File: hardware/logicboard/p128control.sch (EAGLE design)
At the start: 13 parts

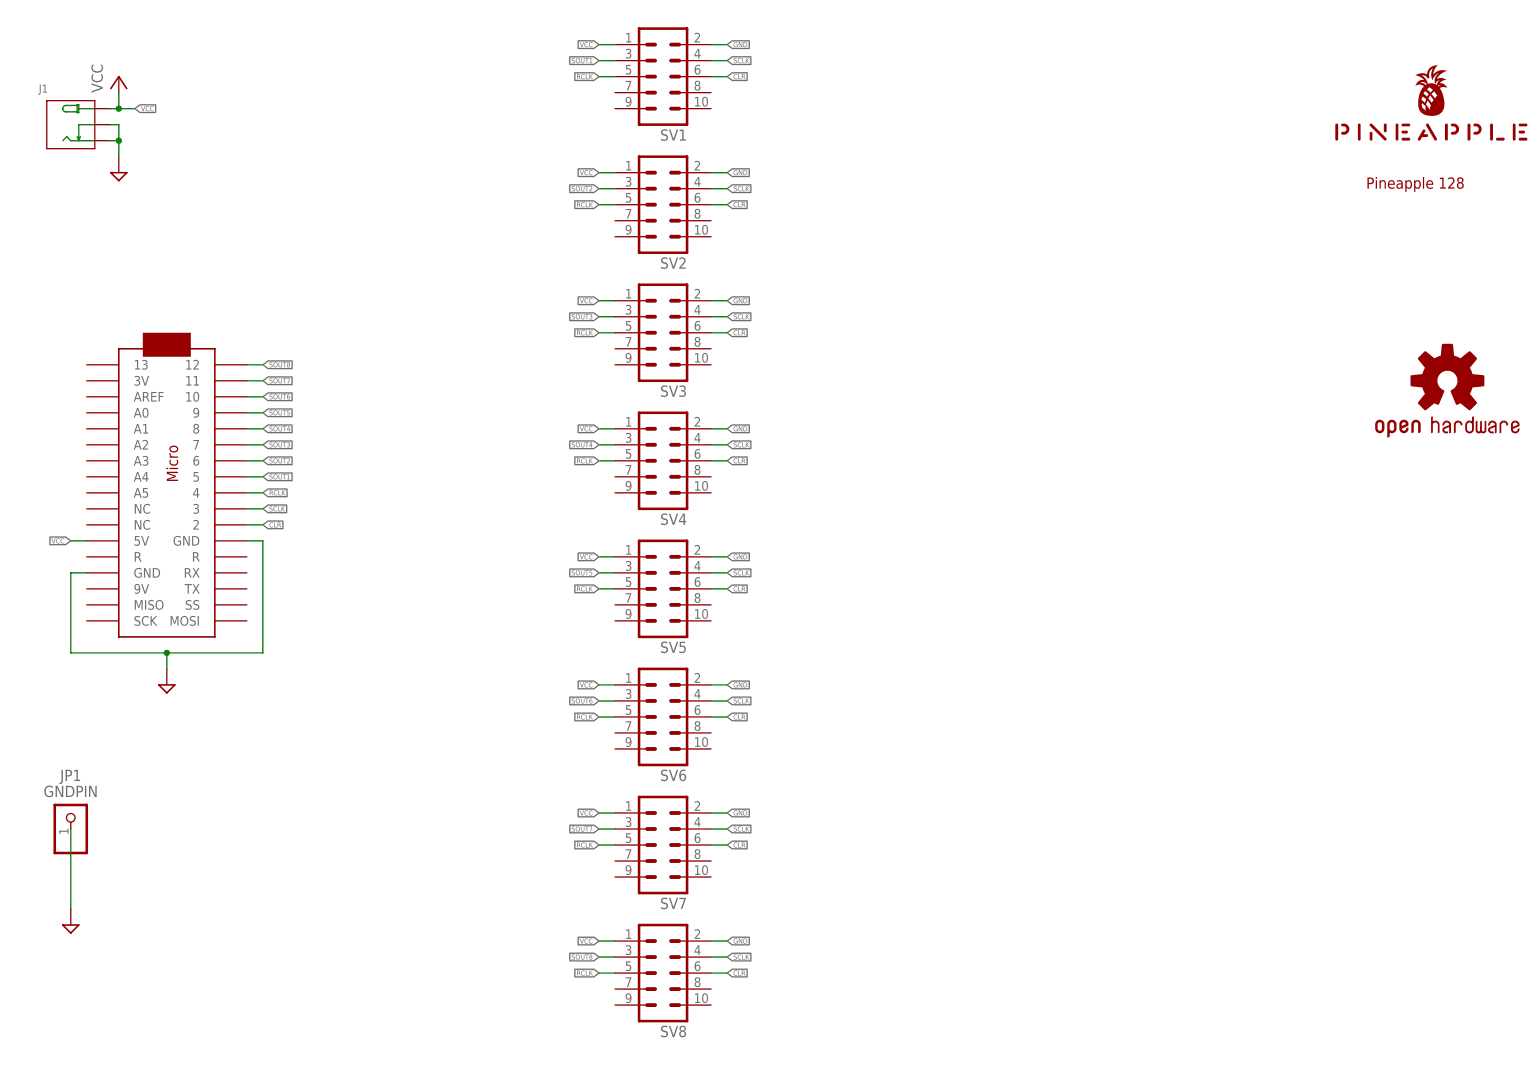
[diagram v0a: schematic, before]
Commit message: Added MIDI-IN.
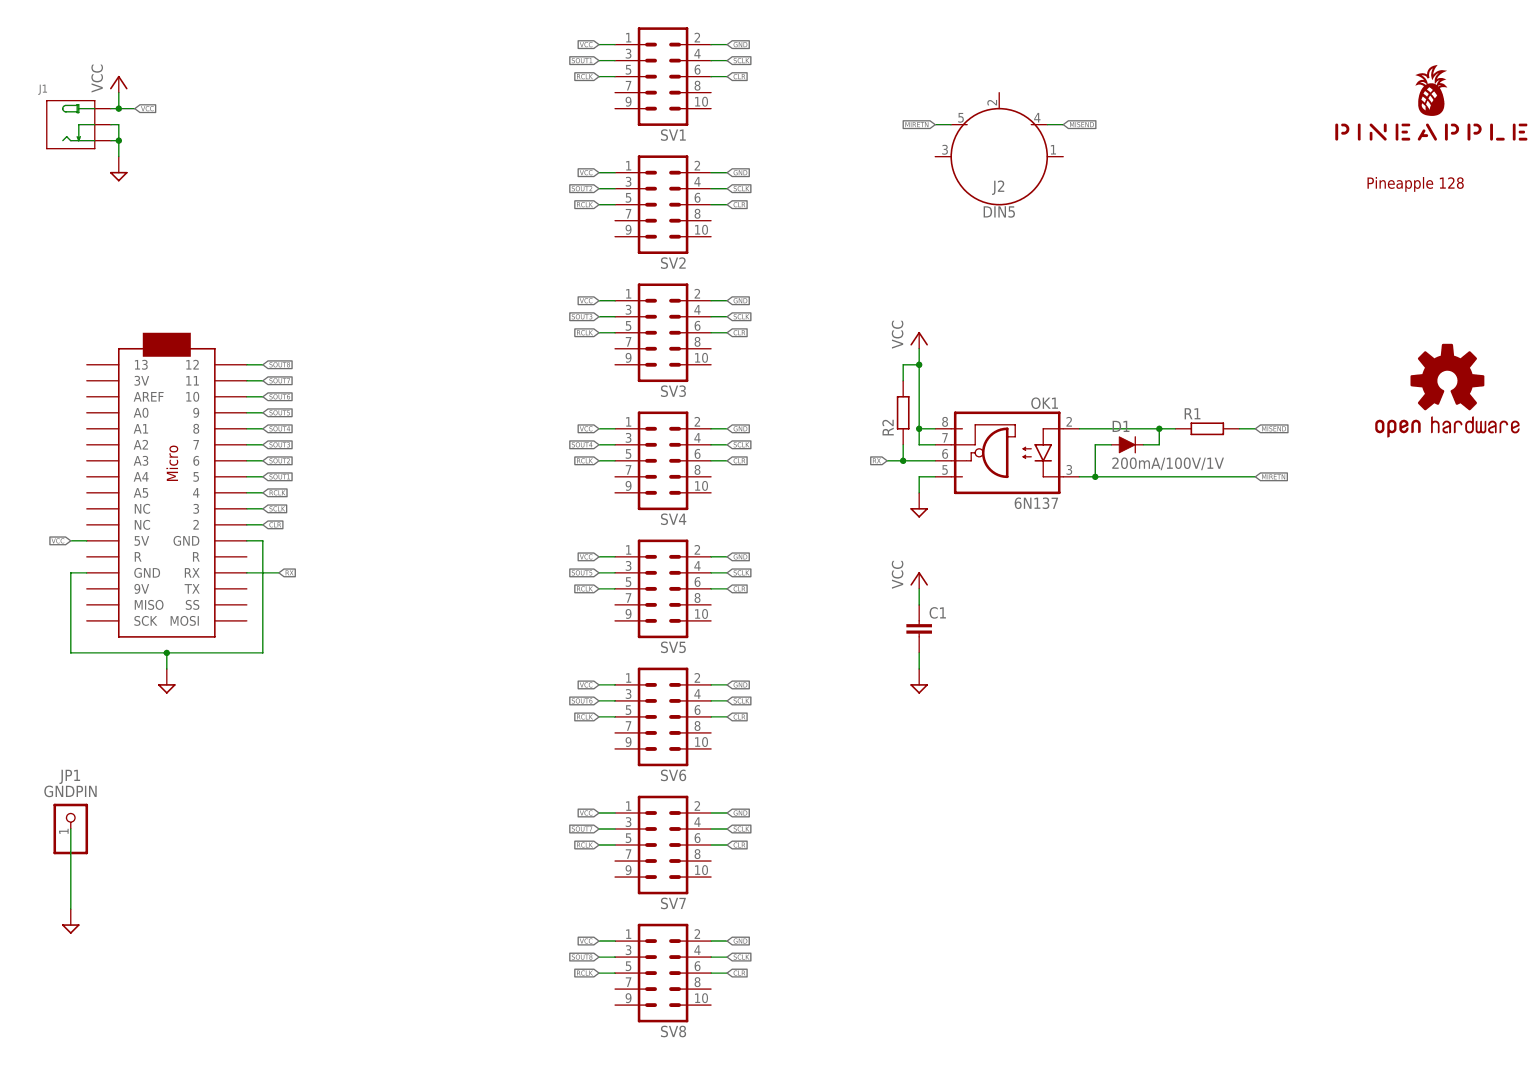
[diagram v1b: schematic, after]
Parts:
- added C1: (no value), resistor:C-EU025-024X044
- added D1: 200mA/100V/1V, SparkFun-DiscreteSemi:DIODE-1N4148
- added J2: DIN5, SparkFun-Connectors:DIN5
- added OK1: 6N137, optocoupler:6N137
- added R1, R2: (no value), resistor:R-EU_0204/5
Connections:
- new net MIRETN: D1.A, J2.5, OK1.C
- new net MISEND: J2.4, R1.2
- new net N$1: D1.C, OK1.A, R1.1
- new net RX: OK1.VO, R2.1, U$2.RX
- net GND: now also C1.2, OK1.GND
- net VCC: now also C1.1, OK1.VCC, OK1.VE, R2.2
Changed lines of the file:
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@@
 <part name="SV7" library="con-ml" library_urn="urn:adsk.eagle:library:164" deviceset="ML10" device="" package3d_urn="urn:adsk.eagle:package:8676/1"/>
 <part name="SV8" library="con-ml" library_urn="urn:adsk.eagle:library:164" deviceset="ML10" device="" package3d_urn="urn:adsk.eagle:package:8676/1"/>
+<part name="J2" library="SparkFun-Connectors" library_urn="urn:adsk.eagle:library:513" deviceset="DIN5" device="" package3d_urn="urn:adsk.eagle:package:38294/1"/>
+<part name="OK1" library="optocoupler" library_urn="urn:adsk.eagle:library:320" deviceset="6N137" device="" package3d_urn="urn:adsk.eagle:package:21941/1"/>
+<part name="D1" library="SparkFun-DiscreteSemi" library_urn="urn:adsk.eagle:library:514" deviceset="DIODE" device="-1N4148" package3d_urn="urn:adsk.eagle:package:38452/1" value="200mA/100V/1V"/>
+<part name="R1" library="resistor" library_urn="urn:adsk.eagle:library:348" deviceset="R-EU_" device="0204/5" package3d_urn="urn:adsk.eagle:package:25955/1"/>
+<part name="R2" library="resistor" library_urn="urn:adsk.eagle:library:348" deviceset="R-EU_" device="0204/5" package3d_urn="urn:adsk.eagle:package:25955/1"/>
+<part name="SUPPLY1" library="supply2" deviceset="GND" device=""/>
+<part name="C1" library="resistor" library_urn="urn:adsk.eagle:library:348" deviceset="C-EU" device="025-024X044" package3d_urn="urn:adsk.eagle:package:26149/1"/>
+<part name="P+2" library="supply1" library_urn="urn:adsk.eagle:library:371" deviceset="VCC" device=""/>
+<part name="P+3" library="supply1" library_urn="urn:adsk.eagle:library:371" deviceset="VCC" device=""/>
+<part name="SUPPLY2" library="supply2" deviceset="GND" device=""/>
 </parts>
 <sheets>
@@
 <attribute name="NAME" x="107.95" y="6.858" size="1.778" layer="95" rot="R180"/>
 </instance>
+<instance part="J2" gate="G$1" x="157.48" y="144.78" smashed="yes">
+<attribute name="NAME" x="157.48" y="139.192" size="1.778" layer="95" font="vector" align="bottom-center"/>
+<attribute name="VALUE" x="157.48" y="136.906" size="1.778" layer="96" font="vector" align="top-center"/>
+</instance>
+<instance part="OK1" gate="A" x="157.48" y="96.52" smashed="yes" rot="MR0">
+<attribute name="NAME" x="167.005" y="104.775" size="1.778" layer="95" rot="MR0"/>
+<attribute name="VALUE" x="167.005" y="88.9" size="1.778" layer="96" rot="MR0"/>
+</instance>
+<instance part="D1" gate="G$1" x="177.8" y="99.06" smashed="yes">
+<attribute name="NAME" x="175.26" y="101.092" size="1.778" layer="95" font="vector"/>
+<attribute name="VALUE" x="175.26" y="97.028" size="1.778" layer="96" font="vector" align="top-left"/>
+</instance>
+<instance part="R1" gate="G$1" x="190.5" y="101.6" smashed="yes">
+<attribute name="NAME" x="186.69" y="103.0986" size="1.778" layer="95"/>
+<attribute name="VALUE" x="186.69" y="98.298" size="1.778" layer="96"/>
+</instance>
+<instance part="R2" gate="G$1" x="142.24" y="104.14" smashed="yes" rot="R90">
+<attribute name="NAME" x="140.7414" y="100.33" size="1.778" layer="95" rot="R90"/>
+<attribute name="VALUE" x="145.542" y="100.33" size="1.778" layer="96" rot="R90"/>
+</instance>
+<instance part="SUPPLY1" gate="GND" x="144.78" y="88.9" smashed="yes"/>
+<instance part="C1" gate="G$1" x="144.78" y="71.12" smashed="yes">
+<attribute name="NAME" x="146.304" y="71.501" size="1.778" layer="95"/>
+<attribute name="VALUE" x="146.304" y="66.421" size="1.778" layer="96"/>
+</instance>
+<instance part="P+2" gate="VCC" x="144.78" y="116.84" smashed="yes">
+<attribute name="VALUE" x="142.24" y="114.3" size="1.778" layer="96" rot="R90"/>
+</instance>
+<instance part="P+3" gate="VCC" x="144.78" y="78.74" smashed="yes">
+<attribute name="VALUE" x="142.24" y="76.2" size="1.778" layer="96" rot="R90"/>
+</instance>
+<instance part="SUPPLY2" gate="GND" x="144.78" y="60.96" smashed="yes"/>
 </instances>
 <busses>
@@
 <label x="114.3" y="20.32" size="0.8128" layer="95" xref="yes"/>
 </segment>
+<segment>
+<pinref part="OK1" gate="A" pin="GND"/>
+<wire x1="147.32" y1="93.98" x2="144.78" y2="93.98" width="0.1524" layer="91"/>
+<wire x1="144.78" y1="93.98" x2="144.78" y2="91.44" width="0.1524" layer="91"/>
+<pinref part="SUPPLY1" gate="GND" pin="GND"/>
+</segment>
+<segment>
+<pinref part="C1" gate="G$1" pin="2"/>
+<pinref part="SUPPLY2" gate="GND" pin="GND"/>
+<wire x1="144.78" y1="66.04" x2="144.78" y2="63.5" width="0.1524" layer="91"/>
+</segment>
 </net>
 <net name="VCC" class="2">
@@
 <label x="93.98" y="20.32" size="0.8128" layer="95" rot="R180" xref="yes"/>
 </segment>
+<segment>
+<pinref part="OK1" gate="A" pin="VCC"/>
+<wire x1="147.32" y1="101.6" x2="144.78" y2="101.6" width="0.1524" layer="91"/>
+<wire x1="144.78" y1="101.6" x2="144.78" y2="99.06" width="0.1524" layer="91"/>
+<pinref part="OK1" gate="A" pin="VE"/>
+<wire x1="144.78" y1="99.06" x2="147.32" y2="99.06" width="0.1524" layer="91"/>
+<wire x1="144.78" y1="101.6" x2="144.78" y2="111.76" width="0.1524" layer="91"/>
+<junction x="144.78" y="101.6"/>
+<pinref part="R2" gate="G$1" pin="2"/>
+<wire x1="144.78" y1="111.76" x2="144.78" y2="114.3" width="0.1524" layer="91"/>
+<wire x1="142.24" y1="109.22" x2="142.24" y2="111.76" width="0.1524" layer="91"/>
+<wire x1="142.24" y1="111.76" x2="144.78" y2="111.76" width="0.1524" layer="91"/>
+<junction x="144.78" y="111.76"/>
+<pinref part="P+2" gate="VCC" pin="VCC"/>
+</segment>
+<segment>
+<pinref part="P+3" gate="VCC" pin="VCC"/>
+<pinref part="C1" gate="G$1" pin="1"/>
+<wire x1="144.78" y1="76.2" x2="144.78" y2="73.66" width="0.1524" layer="91"/>
+</segment>
 </net>
 <net name="CLR" class="0">
@@
 </segment>
 </net>
+<net name="MISEND" class="0">
+<segment>
+<pinref part="J2" gate="G$1" pin="4"/>
+<wire x1="165.1" y1="149.86" x2="167.64" y2="149.86" width="0.1524" layer="91"/>
+<label x="167.64" y="149.86" size="0.8128" layer="95" xref="yes"/>
+</segment>
+<segment>
+<pinref part="R1" gate="G$1" pin="2"/>
+<wire x1="195.58" y1="101.6" x2="198.12" y2="101.6" width="0.1524" layer="91"/>
+<label x="198.12" y="101.6" size="0.8128" layer="95" xref="yes"/>
+</segment>
+</net>
+<net name="MIRETN" class="0">
+<segment>
+<pinref part="J2" gate="G$1" pin="5"/>
+<wire x1="149.86" y1="149.86" x2="147.32" y2="149.86" width="0.1524" layer="91"/>
+<label x="147.32" y="149.86" size="0.8128" layer="95" rot="R180" xref="yes"/>
+</segment>
+<segment>
+<pinref part="D1" gate="G$1" pin="A"/>
+<wire x1="172.72" y1="93.98" x2="198.12" y2="93.98" width="0.1524" layer="91"/>
+<wire x1="175.26" y1="99.06" x2="172.72" y2="99.06" width="0.1524" layer="91"/>
+<wire x1="172.72" y1="99.06" x2="172.72" y2="93.98" width="0.1524" layer="91"/>
+<pinref part="OK1" gate="A" pin="C"/>
+<wire x1="172.72" y1="93.98" x2="170.18" y2="93.98" width="0.1524" layer="91"/>
+<junction x="172.72" y="93.98"/>
+<label x="198.12" y="93.98" size="0.8128" layer="95" xref="yes"/>
+</segment>
+</net>
+<net name="N$1" class="0">
+<segment>
+<pinref part="R1" gate="G$1" pin="1"/>
+<pinref part="OK1" gate="A" pin="A"/>
+<wire x1="185.42" y1="101.6" x2="182.88" y2="101.6" width="0.1524" layer="91"/>
+<pinref part="D1" gate="G$1" pin="C"/>
+<wire x1="182.88" y1="101.6" x2="170.18" y2="101.6" width="0.1524" layer="91"/>
+<wire x1="180.34" y1="99.06" x2="182.88" y2="99.06" width="0.1524" layer="91"/>
+<wire x1="182.88" y1="99.06" x2="182.88" y2="101.6" width="0.1524" layer="91"/>
+<junction x="182.88" y="101.6"/>
+</segment>
+</net>
+<net name="RX" class="0">
+<segment>
+<pinref part="OK1" gate="A" pin="VO"/>
+<wire x1="147.32" y1="96.52" x2="142.24" y2="96.52" width="0.1524" layer="91"/>
+<pinref part="R2" gate="G$1" pin="1"/>
+<wire x1="142.24" y1="96.52" x2="139.7" y2="96.52" width="0.1524" layer="91"/>
+<wire x1="142.24" y1="99.06" x2="142.24" y2="96.52" width="0.1524" layer="91"/>
+<junction x="142.24" y="96.52"/>
+<label x="139.7" y="96.52" size="0.8128" layer="95" rot="R180" xref="yes"/>
+</segment>
+<segment>
+<pinref part="U$2" gate="G$1" pin="RX"/>
+<wire x1="38.1" y1="78.74" x2="43.18" y2="78.74" width="0.1524" layer="91"/>
+<label x="43.18" y="78.74" size="0.8128" layer="95" xref="yes"/>
+</segment>
+</net>

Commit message: Re-designed the controller.
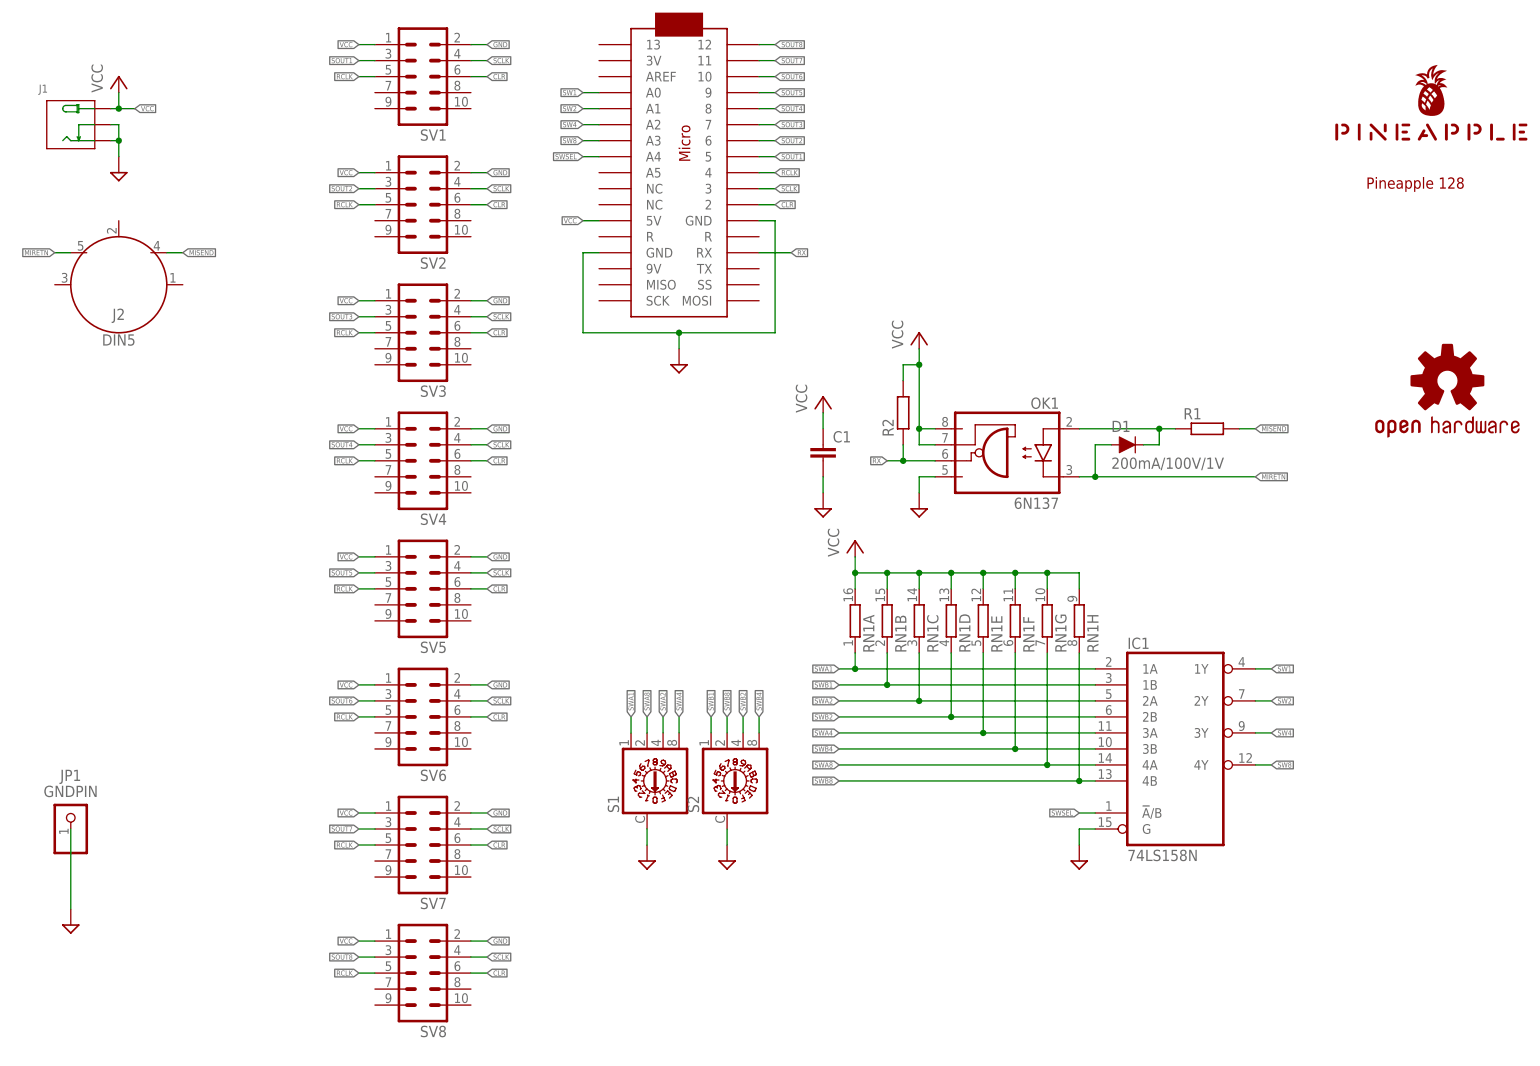
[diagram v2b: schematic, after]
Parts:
- added IC1: 74LS158N, 74xx-us:74LS158N
- added RN1: (no value), resistor-dil:8R-N
- added S1, S2: (no value), switch-dil:A1353HEX
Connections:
- new net SW1: IC1A.1Y, U$2.A0
- new net SW2: IC1A.2Y, U$2.A1
- new net SW4: IC1A.3Y, U$2.A2
- new net SW8: IC1A.4Y, U$2.A3
- new net SWA1: IC1A.1A, RN1A.1, S1.1
- new net SWA2: IC1A.2A, RN1C.1, S1.4
- new net SWA4: IC1A.3A, RN1E.1, S1.8
- new net SWA8: IC1A.4A, RN1G.1, S1.2
- new net SWB1: IC1A.1B, RN1B.1, S2.1
- new net SWB2: IC1A.2B, RN1D.1, S2.4
- new net SWB4: IC1A.3B, RN1F.1, S2.8
- new net SWB8: IC1A.4B, RN1H.1, S2.2
- new net SWSEL: IC1A.!A!/B, U$2.A4
- net GND: now also IC1A.G, S1.C, S2.C
- net VCC: now also RN1A.2, RN1B.2, RN1C.2, RN1D.2, RN1E.2, RN1F.2, RN1G.2, RN1H.2
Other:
- moved on the sheet: C1, J2, SV1, SV2, SV3, SV4, SV5, SV6, SV7, SV8
